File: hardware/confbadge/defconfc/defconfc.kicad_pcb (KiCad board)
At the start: 2 copper layers, 70 x 100 mm, 40 parts, among them J1 Conn_02x03_Odd_Even, J2 Conn_02x03_Odd_Even, SW1 SW_SPST, SW2 SW_SPST, SW3 SW_SPST, SW4 SW_SPDT, U1 M24SR16-YMN6T/2, U2 M24SR16-YMN6T/2, U3 ATTINY13A-SSU

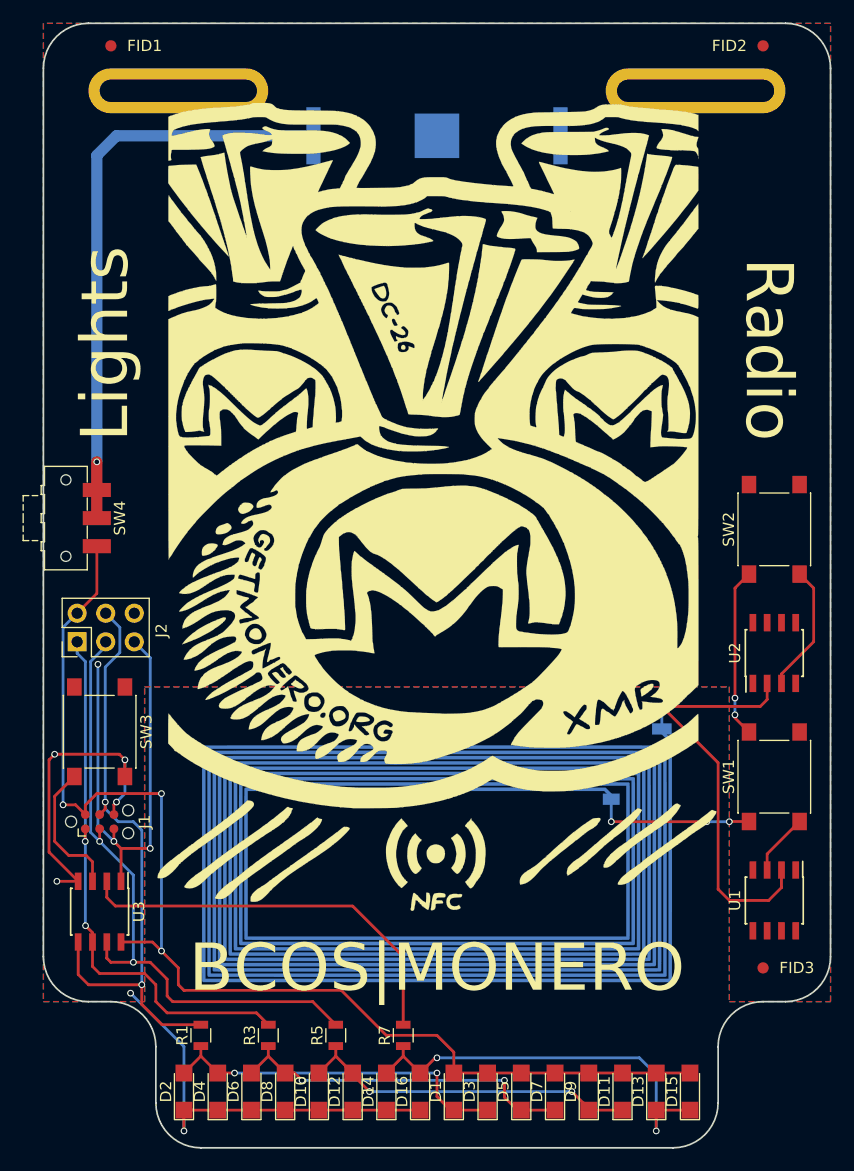
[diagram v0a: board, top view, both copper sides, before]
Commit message: Cleaned out unversioned graphic elements from hardware design.
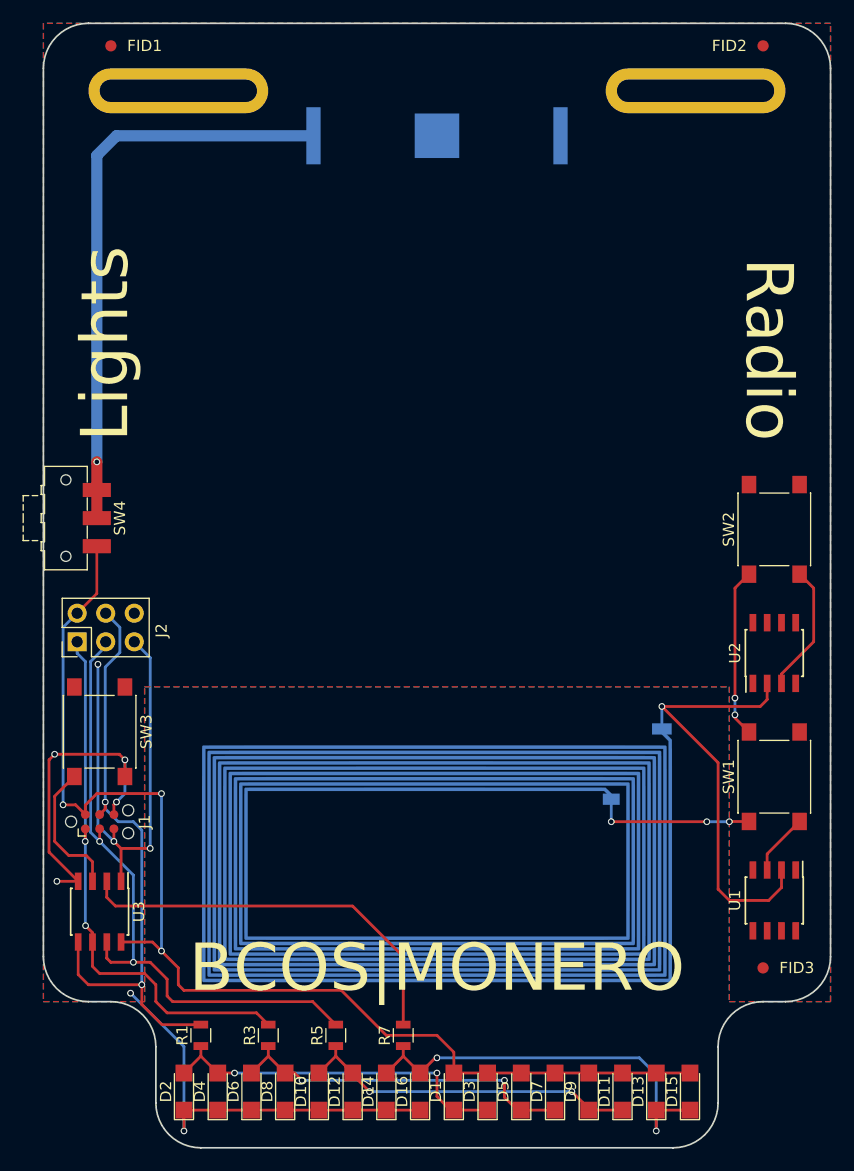
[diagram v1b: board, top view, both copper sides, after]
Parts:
- removed L1: Graphbrand, Monero_HW:Brandgraphicsfront
